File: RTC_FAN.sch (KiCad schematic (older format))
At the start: 13 parts, among them J3 Conn_01x02, Q2 MCH3481-TL-W, U8 DS3231S#, U9 BU2032SM-HD-G

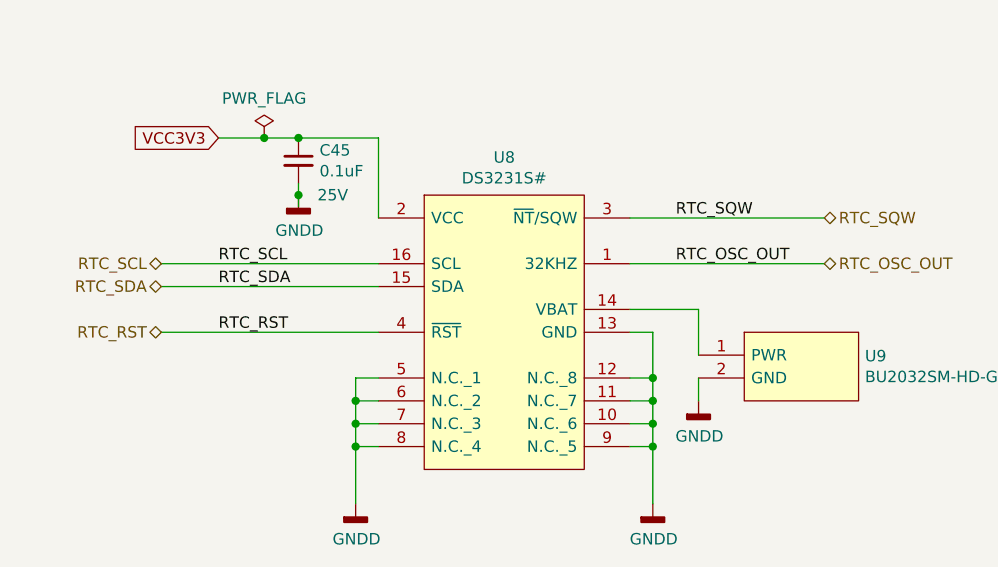
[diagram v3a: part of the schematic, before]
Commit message: Connections were made to FPGA banks
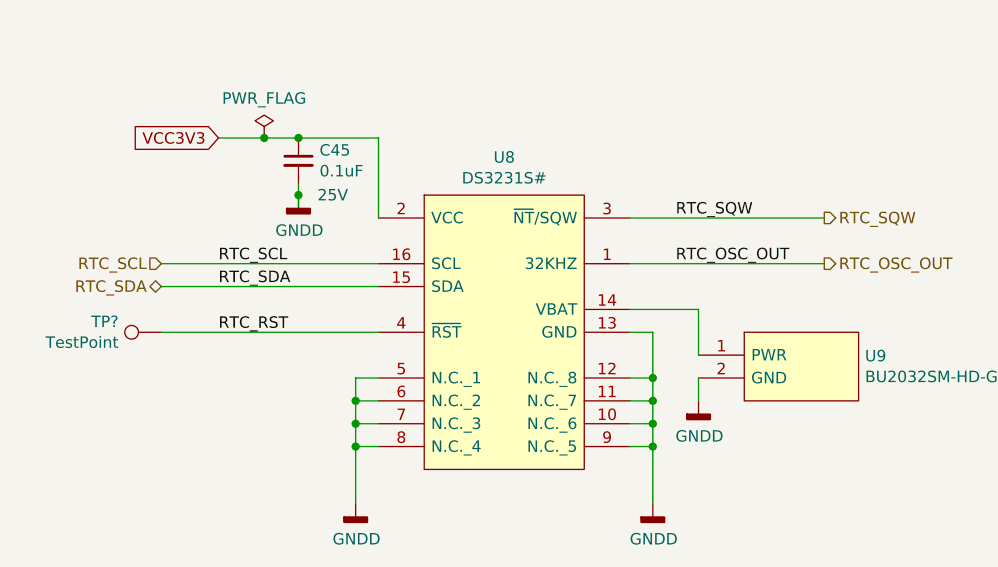
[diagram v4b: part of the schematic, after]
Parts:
- added TP?: TestPoint, TestPoint:TestPoint_Pad_2.0x2.0mm, symbol Connector:TestPoint
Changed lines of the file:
@@
 $Descr A4 11693 8268
 encoding utf-8
-Sheet 10 25
+Sheet 8 25
 Title "CGMPCX1006"
 Date "2021-02-03"
@@
 	1    0    0    -1
 $EndComp
-Text HLabel 2250 3300 0    50   BiDi ~ 0
+Text HLabel 2250 3300 0    50   Input ~ 0
 RTC_SCL
 Text HLabel 2250 3400 0    50   BiDi ~ 0
 RTC_SDA
-Text HLabel 2250 3600 0    50   BiDi ~ 0
-RTC_RST
-Text HLabel 5150 3300 2    50   BiDi ~ 0
+Text HLabel 5150 3300 2    50   Output ~ 0
 RTC_OSC_OUT
-Text HLabel 5150 3100 2    50   BiDi ~ 0
+Text HLabel 5150 3100 2    50   Output ~ 0
 RTC_SQW
 Text HLabel 7400 3800 0    50   Input ~ 0
@@
 Text HLabel 8650 2800 0    157  Input ~ 0
 12VIN
+$Comp
+L Connector:TestPoint TP?
+U 1 1 6078253D
+P 2250 3600
+AR Path="/6078253D" Ref="TP?"  Part="1"
+AR Path="/601E7CC8/6078253D" Ref="TP?"  Part="1"
+F 0 "TP?" V 2296 3787 50  0000 L CNN
+F 1 "TestPoint" V 2205 3787 50  0000 L CNN
+F 2 "TestPoint:TestPoint_Pad_2.0x2.0mm" H 2450 3600 50  0001 C CNN
+F 3 "~" H 2450 3600 50  0001 C CNN
+	1    2250 3600
+	0    -1   -1   0
+$EndComp
 $EndSCHEMATC

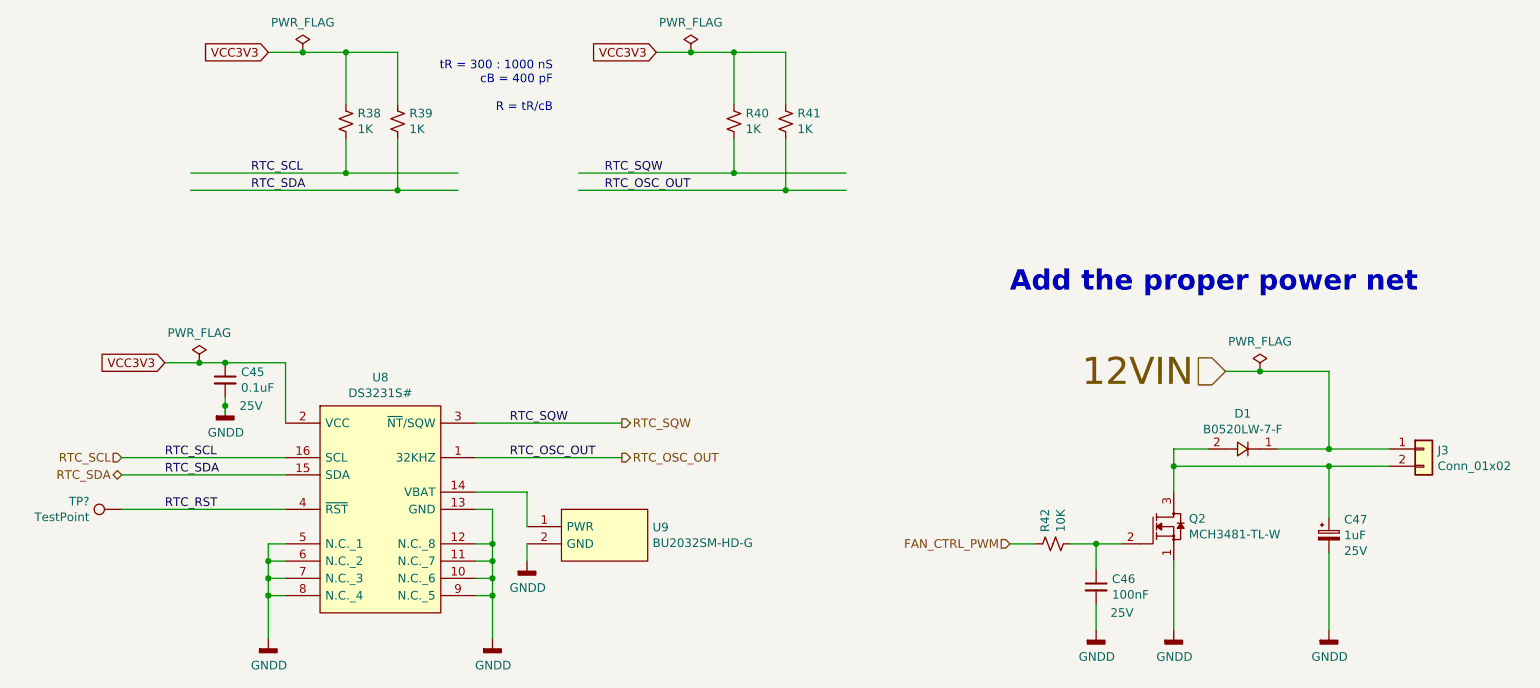
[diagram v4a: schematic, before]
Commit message: Corrected PCB import errors
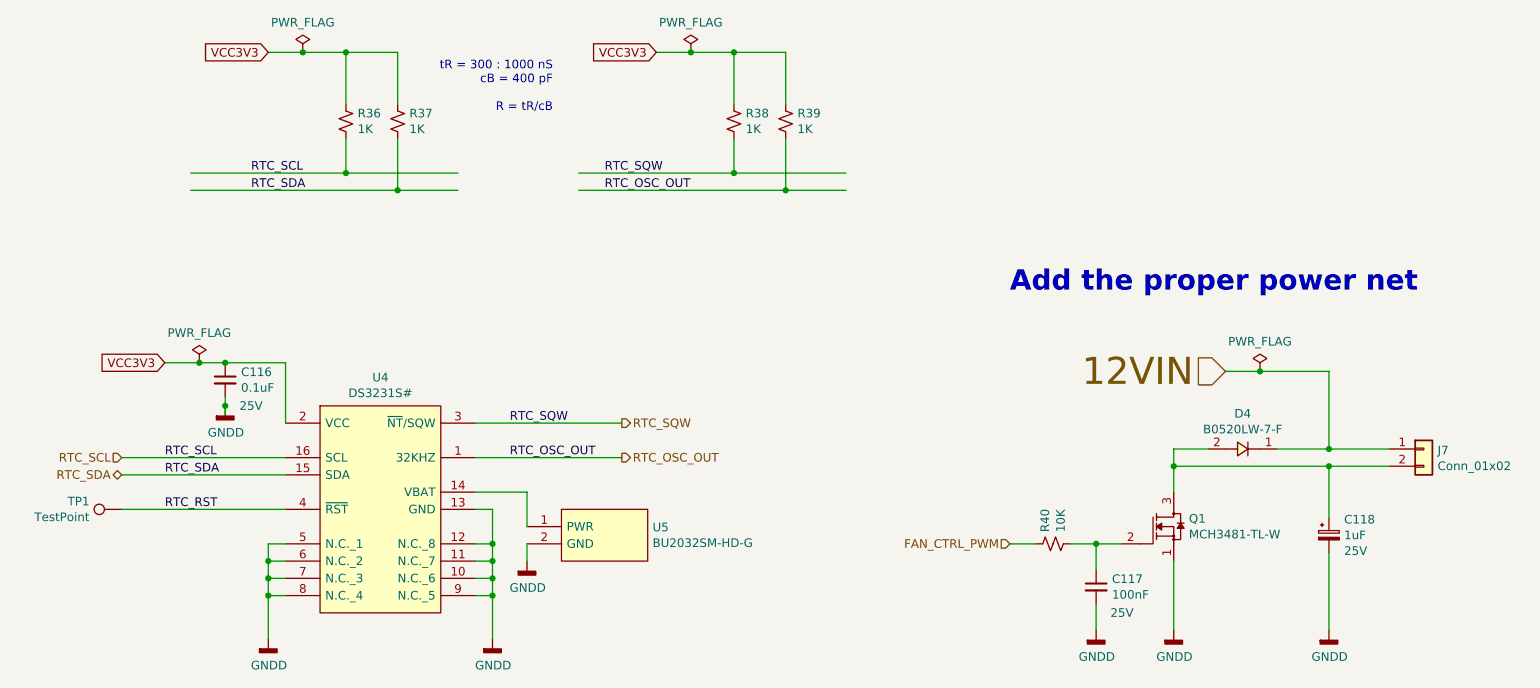
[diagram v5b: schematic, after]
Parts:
- gave numbers to parts that had none: 1
- renumbered C45 to C116, C46 to C117, C47 to C118, D1 to D4, J3 to J7, Q2 to Q1, R38 to R36, R39 to R37, R40 to R38, R41 to R39, R42 to R40, U8 to U4, U9 to U5
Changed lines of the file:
@@
 $EndDescr
 $Comp
-L GM_Clock_n_Timers:DS3231S# U8
+L GM_Clock_n_Timers:DS3231S# U4
 U 1 1 60229CED
 P 3400 3000
-F 0 "U8" H 3750 3165 50  0000 C CNN
+F 0 "U4" H 3750 3165 50  0000 C CNN
 F 1 "DS3231S#" H 3750 3074 50  0000 C CNN
 F 2 "SOIC127P1032X265-16N" H 4850 2700 50  0001 L CNN
@@
 AR Path="/601DF0A6/6022EFDE" Ref="#PWR?"  Part="1"
 AR Path="/601E7C5A/6022EFDE" Ref="#PWR?"  Part="1"
-AR Path="/601E7CC8/6022EFDE" Ref="#PWR029"  Part="1"
-F 0 "#PWR029" H 3100 4100 50  0001 C CNN
+AR Path="/601E7CC8/6022EFDE" Ref="#PWR049"  Part="1"
+F 0 "#PWR049" H 3100 4100 50  0001 C CNN
 F 1 "GNDD" H 3104 4195 50  0000 C CNN
 F 2 "" H 3100 4350 50  0001 C CNN
@@
 AR Path="/601DF0A6/6022F29E" Ref="#PWR?"  Part="1"
 AR Path="/601E7C5A/6022F29E" Ref="#PWR?"  Part="1"
-AR Path="/601E7CC8/6022F29E" Ref="#PWR030"  Part="1"
-F 0 "#PWR030" H 4400 4100 50  0001 C CNN
+AR Path="/601E7CC8/6022F29E" Ref="#PWR050"  Part="1"
+F 0 "#PWR050" H 4400 4100 50  0001 C CNN
 F 1 "GNDD" H 4404 4195 50  0000 C CNN
 F 2 "" H 4400 4350 50  0001 C CNN
@@
 P 2700 2750
 AR Path="/601E7C5A/6023071D" Ref="#FLG?"  Part="1"
-AR Path="/601E7CC8/6023071D" Ref="#FLG016"  Part="1"
-F 0 "#FLG016" H 2700 2825 50  0001 C CNN
+AR Path="/601E7CC8/6023071D" Ref="#FLG013"  Part="1"
+F 0 "#FLG013" H 2700 2825 50  0001 C CNN
 F 1 "PWR_FLAG" H 2700 2923 50  0000 C CNN
 F 2 "" H 2700 2750 50  0001 C CNN
@@
 P 2850 2850
 AR Path="/601E7C5A/60231765" Ref="C?"  Part="1"
-AR Path="/601E7CC8/60231765" Ref="C45"  Part="1"
-F 0 "C45" H 2942 2896 50  0000 L CNN
+AR Path="/601E7CC8/60231765" Ref="C116"  Part="1"
+F 0 "C116" H 2942 2896 50  0000 L CNN
 F 1 "0.1uF" H 2942 2805 50  0000 L CNN
 F 2 "Capacitor_SMD:C_0603_1608Metric_Pad1.08x0.95mm_HandSolder" H 2850 2850 50  0001 C CNN
@@
 AR Path="/601DF0A6/6023262F" Ref="#PWR?"  Part="1"
 AR Path="/601E7C5A/6023262F" Ref="#PWR?"  Part="1"
-AR Path="/601E7CC8/6023262F" Ref="#PWR028"  Part="1"
-F 0 "#PWR028" H 2850 2750 50  0001 C CNN
+AR Path="/601E7CC8/6023262F" Ref="#PWR048"  Part="1"
+F 0 "#PWR048" H 2850 2750 50  0001 C CNN
 F 1 "GNDD" H 2854 2845 50  0000 C CNN
 F 2 "" H 2850 3000 50  0001 C CNN
@@
 P 3300 950
 AR Path="/601E7C5A/602351EC" Ref="#FLG?"  Part="1"
-AR Path="/601E7CC8/602351EC" Ref="#FLG017"  Part="1"
-F 0 "#FLG017" H 3300 1025 50  0001 C CNN
+AR Path="/601E7CC8/602351EC" Ref="#FLG014"  Part="1"
+F 0 "#FLG014" H 3300 1025 50  0001 C CNN
 F 1 "PWR_FLAG" H 3300 1123 50  0000 C CNN
 F 2 "" H 3300 950 50  0001 C CNN
@@
 P 3550 1350
 AR Path="/601E7C5A/60235A7C" Ref="R?"  Part="1"
-AR Path="/601E7CC8/60235A7C" Ref="R38"  Part="1"
-F 0 "R38" H 3618 1396 50  0000 L CNN
+AR Path="/601E7CC8/60235A7C" Ref="R36"  Part="1"
+F 0 "R36" H 3618 1396 50  0000 L CNN
 F 1 "1K" H 3618 1305 50  0000 L CNN
 F 2 "Resistor_SMD:R_0603_1608Metric_Pad0.98x0.95mm_HandSolder" H 3550 1350 50  0001 C CNN
@@
 P 3850 1350
 AR Path="/601E7C5A/60236293" Ref="R?"  Part="1"
-AR Path="/601E7CC8/60236293" Ref="R39"  Part="1"
-F 0 "R39" H 3918 1396 50  0000 L CNN
+AR Path="/601E7CC8/60236293" Ref="R37"  Part="1"
+F 0 "R37" H 3918 1396 50  0000 L CNN
 F 1 "1K" H 3918 1305 50  0000 L CNN
 F 2 "Resistor_SMD:R_0603_1608Metric_Pad0.98x0.95mm_HandSolder" H 3850 1350 50  0001 C CNN
@@
 P 5550 950
 AR Path="/601E7C5A/6024882C" Ref="#FLG?"  Part="1"
-AR Path="/601E7CC8/6024882C" Ref="#FLG018"  Part="1"
-F 0 "#FLG018" H 5550 1025 50  0001 C CNN
+AR Path="/601E7CC8/6024882C" Ref="#FLG015"  Part="1"
+F 0 "#FLG015" H 5550 1025 50  0001 C CNN
 F 1 "PWR_FLAG" H 5550 1123 50  0000 C CNN
 F 2 "" H 5550 950 50  0001 C CNN
@@
 P 5800 1350
 AR Path="/601E7C5A/60248834" Ref="R?"  Part="1"
-AR Path="/601E7CC8/60248834" Ref="R40"  Part="1"
-F 0 "R40" H 5868 1396 50  0000 L CNN
+AR Path="/601E7CC8/60248834" Ref="R38"  Part="1"
+F 0 "R38" H 5868 1396 50  0000 L CNN
 F 1 "1K" H 5868 1305 50  0000 L CNN
 F 2 "Resistor_SMD:R_0603_1608Metric_Pad0.98x0.95mm_HandSolder" H 5800 1350 50  0001 C CNN
@@
 P 6100 1350
 AR Path="/601E7C5A/6024883A" Ref="R?"  Part="1"
-AR Path="/601E7CC8/6024883A" Ref="R41"  Part="1"
-F 0 "R41" H 6168 1396 50  0000 L CNN
+AR Path="/601E7CC8/6024883A" Ref="R39"  Part="1"
+F 0 "R39" H 6168 1396 50  0000 L CNN
 F 1 "1K" H 6168 1305 50  0000 L CNN
 F 2 "Resistor_SMD:R_0603_1608Metric_Pad0.98x0.95mm_HandSolder" H 6100 1350 50  0001 C CNN
@@
 AR Path="/601DF0A6/6025F3F3" Ref="#PWR?"  Part="1"
 AR Path="/601E7C5A/6025F3F3" Ref="#PWR?"  Part="1"
-AR Path="/601E7CC8/6025F3F3" Ref="#PWR031"  Part="1"
-F 0 "#PWR031" H 4600 3650 50  0001 C CNN
+AR Path="/601E7CC8/6025F3F3" Ref="#PWR051"  Part="1"
+F 0 "#PWR051" H 4600 3650 50  0001 C CNN
 F 1 "GNDD" H 4604 3745 50  0000 C CNN
 F 2 "" H 4600 3900 50  0001 C CNN
@@
 $EndComp
 $Comp
-L GM_Battery_Holders_n_Contacts:BU2032SM-HD-G U9
+L GM_Battery_Holders_n_Contacts:BU2032SM-HD-G U5
 U 1 1 6022F346
 P 4800 3600
-F 0 "U9" H 5328 3496 50  0000 L CNN
+F 0 "U5" H 5328 3496 50  0000 L CNN
 F 1 "BU2032SM-HD-G" H 5328 3405 50  0000 L CNN
 F 2 "BU2032SM-HD-G" H 5450 3700 50  0001 L CNN
@@
 	4600 3500 4300 3500
 $Comp
-L GM_MOSFET:MCH3481-TL-W Q2
+L GM_MOSFET:MCH3481-TL-W Q1
 U 1 1 602539F0
 P 8250 3700
-F 0 "Q2" H 8438 3746 50  0000 L CNN
+F 0 "Q1" H 8438 3746 50  0000 L CNN
 F 1 "MCH3481-TL-W" H 8438 3655 50  0000 L CNN
 F 2 "GM_SOT:SOT65P270X085-3N" H 9250 3900 50  0001 C CNN
@@
 P 7650 3800
 AR Path="/601E7C5A/60254F0F" Ref="R?"  Part="1"
-AR Path="/601E7CC8/60254F0F" Ref="R42"  Part="1"
-F 0 "R42" H 7718 3846 50  0000 L CNN
+AR Path="/601E7CC8/60254F0F" Ref="R40"  Part="1"
+F 0 "R40" H 7718 3846 50  0000 L CNN
 F 1 "10K" H 7718 3755 50  0000 L CNN
 F 2 "Resistor_SMD:R_0603_1608Metric_Pad0.98x0.95mm_HandSolder" H 7650 3800 50  0001 C CNN
@@
 P 7900 4050
 AR Path="/601E7C5A/60254F16" Ref="C?"  Part="1"
-AR Path="/601E7CC8/60254F16" Ref="C46"  Part="1"
-F 0 "C46" H 7992 4096 50  0000 L CNN
+AR Path="/601E7CC8/60254F16" Ref="C117"  Part="1"
+F 0 "C117" H 7992 4096 50  0000 L CNN
 F 1 "100nF" H 7992 4005 50  0000 L CNN
 F 2 "Capacitor_SMD:C_0603_1608Metric_Pad1.08x0.95mm_HandSolder" H 7900 4050 50  0001 C CNN
@@
 AR Path="/601DF0A6/6025D5E9" Ref="#PWR?"  Part="1"
 AR Path="/601E7C5A/6025D5E9" Ref="#PWR?"  Part="1"
-AR Path="/601E7CC8/6025D5E9" Ref="#PWR032"  Part="1"
-F 0 "#PWR032" H 7900 4050 50  0001 C CNN
+AR Path="/601E7CC8/6025D5E9" Ref="#PWR052"  Part="1"
+F 0 "#PWR052" H 7900 4050 50  0001 C CNN
 F 1 "GNDD" H 7904 4145 50  0000 C CNN
 F 2 "" H 7900 4300 50  0001 C CNN
@@
 AR Path="/601DF0A6/60263673" Ref="#PWR?"  Part="1"
 AR Path="/601E7C5A/60263673" Ref="#PWR?"  Part="1"
-AR Path="/601E7CC8/60263673" Ref="#PWR033"  Part="1"
-F 0 "#PWR033" H 8350 4050 50  0001 C CNN
+AR Path="/601E7CC8/60263673" Ref="#PWR053"  Part="1"
+F 0 "#PWR053" H 8350 4050 50  0001 C CNN
 F 1 "GNDD" H 8354 4145 50  0000 C CNN
 F 2 "" H 8350 4300 50  0001 C CNN
@@
 $EndComp
 $Comp
-L Device:C_Polarized_Small C47
+L Device:C_Polarized_Small C118
 U 1 1 60269FC6
 P 9250 3750
-F 0 "C47" H 9338 3841 50  0000 L CNN
+F 0 "C118" H 9338 3841 50  0000 L CNN
 F 1 "1uF" H 9338 3750 50  0000 L CNN
 F 2 "Capacitor_Tantalum_SMD:CP_EIA-1608-10_AVX-L_Pad1.25x1.05mm_HandSolder" H 9250 3750 50  0001 C CNN
@@
 $EndComp
 $Comp
-L Connector_Generic:Conn_01x02 J3
+L Connector_Generic:Conn_01x02 J7
 U 1 1 60278B21
 P 9800 3250
-F 0 "J3" H 9880 3242 50  0000 L CNN
+F 0 "J7" H 9880 3242 50  0000 L CNN
 F 1 "Conn_01x02" H 9880 3151 50  0000 L CNN
 F 2 "Connector_PinHeader_1.27mm:PinHeader_1x02_P1.27mm_Vertical" H 9800 3250 50  0001 C CNN
@@
 AR Path="/601DF0A6/6028129F" Ref="#PWR?"  Part="1"
 AR Path="/601E7C5A/6028129F" Ref="#PWR?"  Part="1"
-AR Path="/601E7CC8/6028129F" Ref="#PWR034"  Part="1"
-F 0 "#PWR034" H 9250 4050 50  0001 C CNN
+AR Path="/601E7CC8/6028129F" Ref="#PWR054"  Part="1"
+F 0 "#PWR054" H 9250 4050 50  0001 C CNN
 F 1 "GNDD" H 9254 4145 50  0000 C CNN
 F 2 "" H 9250 4300 50  0001 C CNN
@@
 	7550 3800 7400 3800
 $Comp
-L GM_Diodes:B0520LW-7-F D1
+L GM_Diodes:B0520LW-7-F D4
 U 1 1 6029EC80
 P 8750 3250
-F 0 "D1" H 8750 3045 50  0000 C CNN
+F 0 "D4" H 8750 3045 50  0000 C CNN
 F 1 "B0520LW-7-F" H 8750 3136 50  0000 C CNN
 F 2 "SOD3716X145N" H 9250 3250 50  0001 L CNN
@@
 P 8850 2800
 AR Path="/601E7C5A/602A4D12" Ref="#FLG?"  Part="1"
-AR Path="/601E7CC8/602A4D12" Ref="#FLG019"  Part="1"
-F 0 "#FLG019" H 8850 2875 50  0001 C CNN
+AR Path="/601E7CC8/602A4D12" Ref="#FLG016"  Part="1"
+F 0 "#FLG016" H 8850 2875 50  0001 C CNN
 F 1 "PWR_FLAG" H 8850 2973 50  0000 C CNN
 F 2 "" H 8850 2800 50  0001 C CNN
@@
 P 2250 3600
 AR Path="/6078253D" Ref="TP?"  Part="1"
-AR Path="/601E7CC8/6078253D" Ref="TP?"  Part="1"
-F 0 "TP?" V 2296 3787 50  0000 L CNN
+AR Path="/601E7CC8/6078253D" Ref="TP1"  Part="1"
+F 0 "TP1" V 2296 3787 50  0000 L CNN
 F 1 "TestPoint" V 2205 3787 50  0000 L CNN
 F 2 "TestPoint:TestPoint_Pad_2.0x2.0mm" H 2450 3600 50  0001 C CNN
